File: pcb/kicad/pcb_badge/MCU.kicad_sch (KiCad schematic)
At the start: 63 parts, among them J3 Conn_01x04_Pin, J4 Conn_01x03_Pin, J5 Conn_01x03_Pin, J7 Conn_01x02_Pin, Q9 2N7002, SW1 SW_MEC_5E, SW2 SW_MEC_5E, SW3 SW_MEC_5E, SW4 SW_MEC_5E, SW5 SW_MEC_5E, SW6 SW_MEC_5E, SW7 SW_MEC_5E, SW8 SW_MEC_5E, U3 STM32F103CBT6, U5 LSM6DS3TR-C, U6 IRM-H638T/TR2, Y1 TAXM8M4RFDCET2T

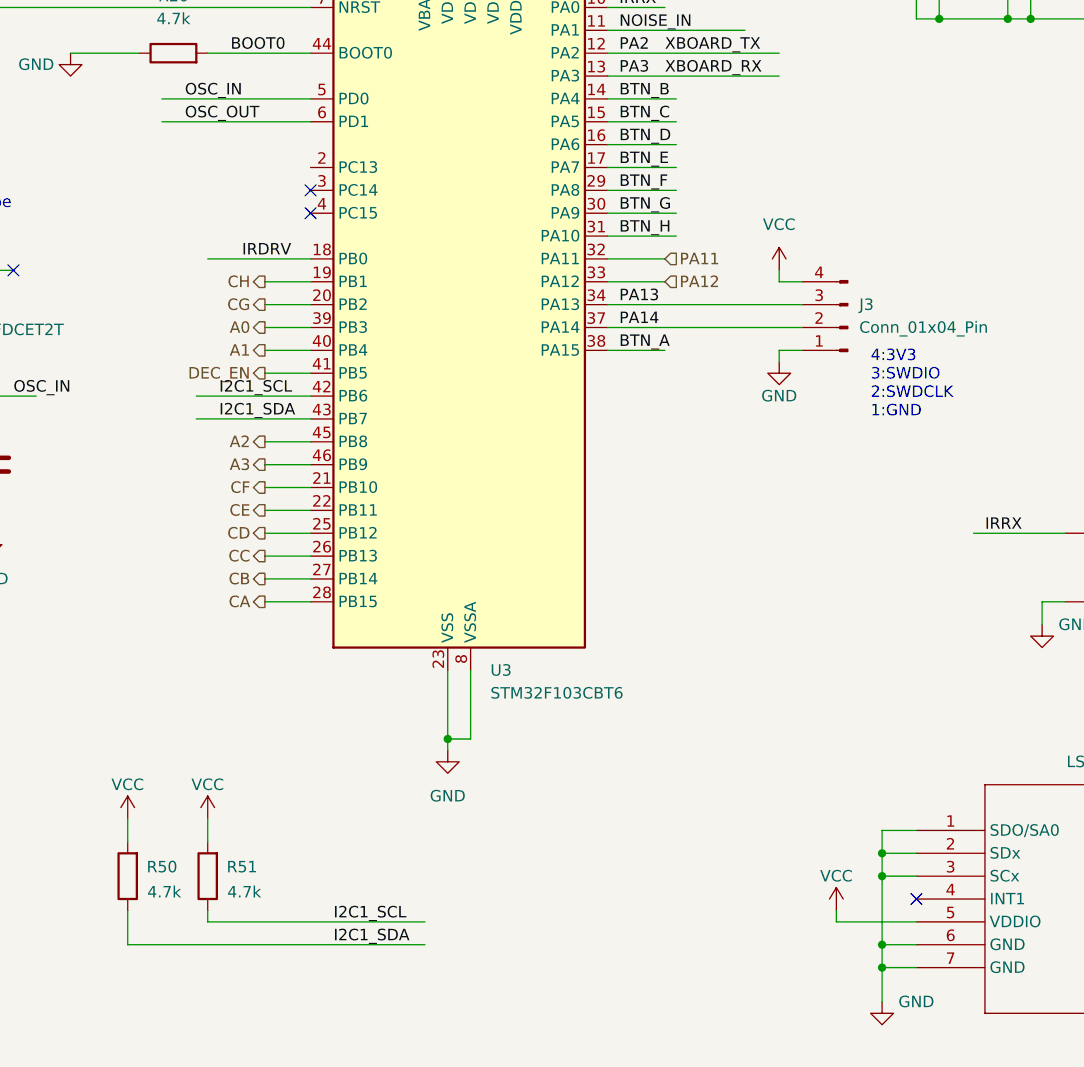
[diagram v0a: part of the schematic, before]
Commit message: pcb: Connect accelerometer INT1
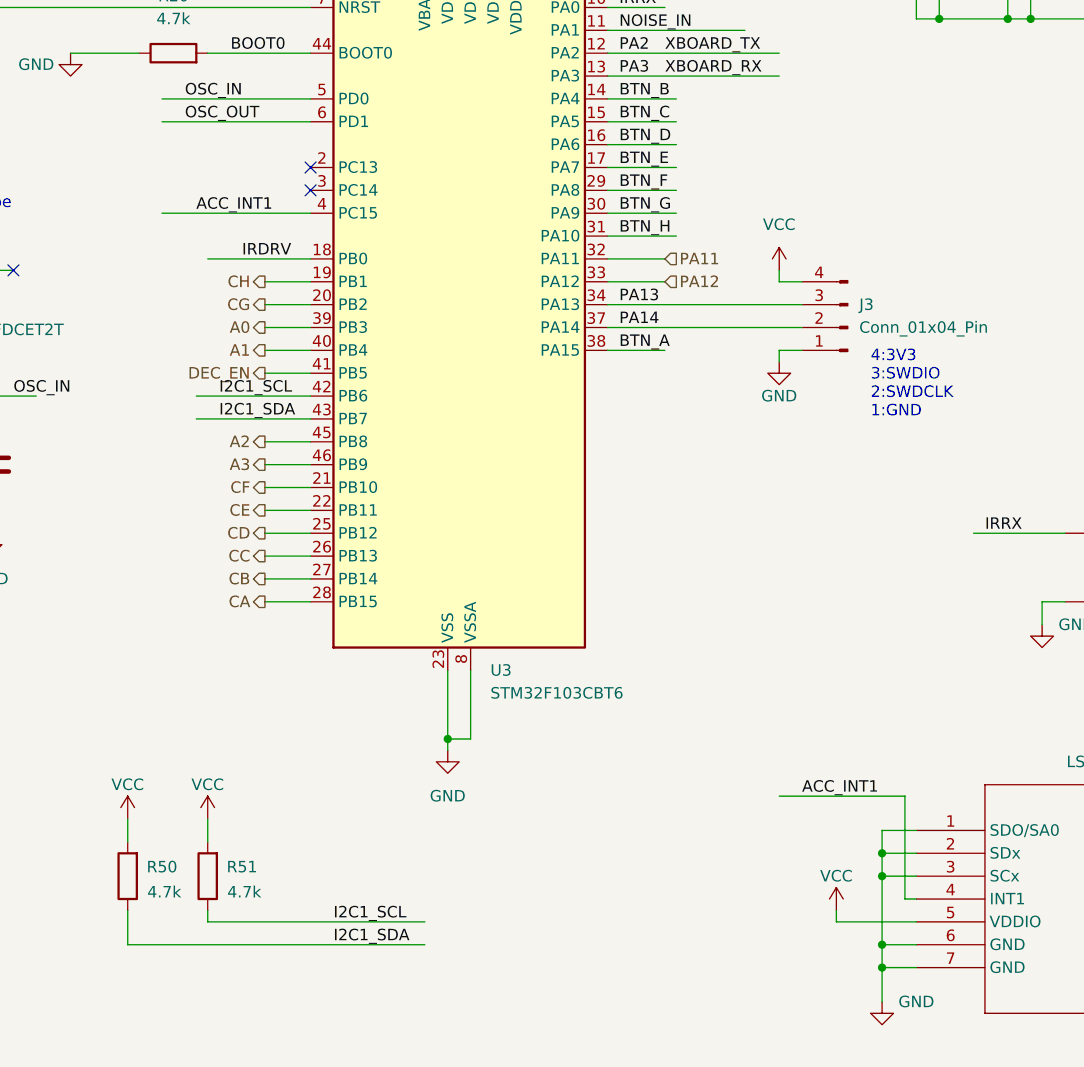
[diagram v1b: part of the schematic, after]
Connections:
- net ACC_INT1: now reaches U5.4 (INT1)
- net ACC_INT1: now also U3.4 (PC15)
- no-connect marks 7 -> 6
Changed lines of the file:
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@@
 	)
 	(no_connect
-		(at 121.92 87.63)
-	)
-	(no_connect
-		(at 189.23 163.83)
+		(at 121.92 82.55)
 	)
 	(no_connect
@@
 	(wire
 		(pts
+			(xy 105.41 87.63) (xy 121.92 87.63)
+		)
+		(stroke
+			(width 0)
+			(type default)
+		)
+	)
+	(wire
+		(pts
 			(xy 44.45 107.95) (xy 44.45 99.06)
 		)
@@
 	(wire
 		(pts
+			(xy 189.23 163.83) (xy 187.96 163.83)
+		)
+		(stroke
+			(width 0)
+			(type default)
+		)
+	)
+	(wire
+		(pts
 			(xy 134.62 200.66) (xy 142.24 200.66)
 		)
@@
 	(wire
 		(pts
+			(xy 173.99 152.4) (xy 187.96 152.4)
+		)
+		(stroke
+			(width 0)
+			(type default)
+		)
+	)
+	(wire
+		(pts
 			(xy 154.94 100.33) (xy 176.53 100.33)
 		)
@@
 		(pts
 			(xy 209.55 50.8) (xy 212.09 50.8)
+		)
+		(stroke
+			(width 0)
+			(type default)
+		)
+	)
+	(wire
+		(pts
+			(xy 187.96 163.83) (xy 187.96 152.4)
 		)
 		(stroke
@@
 		)
 	)
+	(label "ACC_INT1"
+		(at 109.22 87.63 0)
+		(effects
+			(font
+				(size 1.27 1.27)
+			)
+			(justify left bottom)
+		)
+	)
 	(label "BTN_H"
 		(at 260.35 50.8 0)
@@
 		(effects
 			(font
+				(size 1.27 1.27)
+			)
+			(justify left bottom)
+		)
+	)
+	(label "ACC_INT1"
+		(at 176.53 152.4 0)
+		(effects
+			(font
